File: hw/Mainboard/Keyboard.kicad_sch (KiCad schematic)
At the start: 8 parts, among them J18 KEYBOARD, J19 KEYBOARD_EX, U19 74LS145

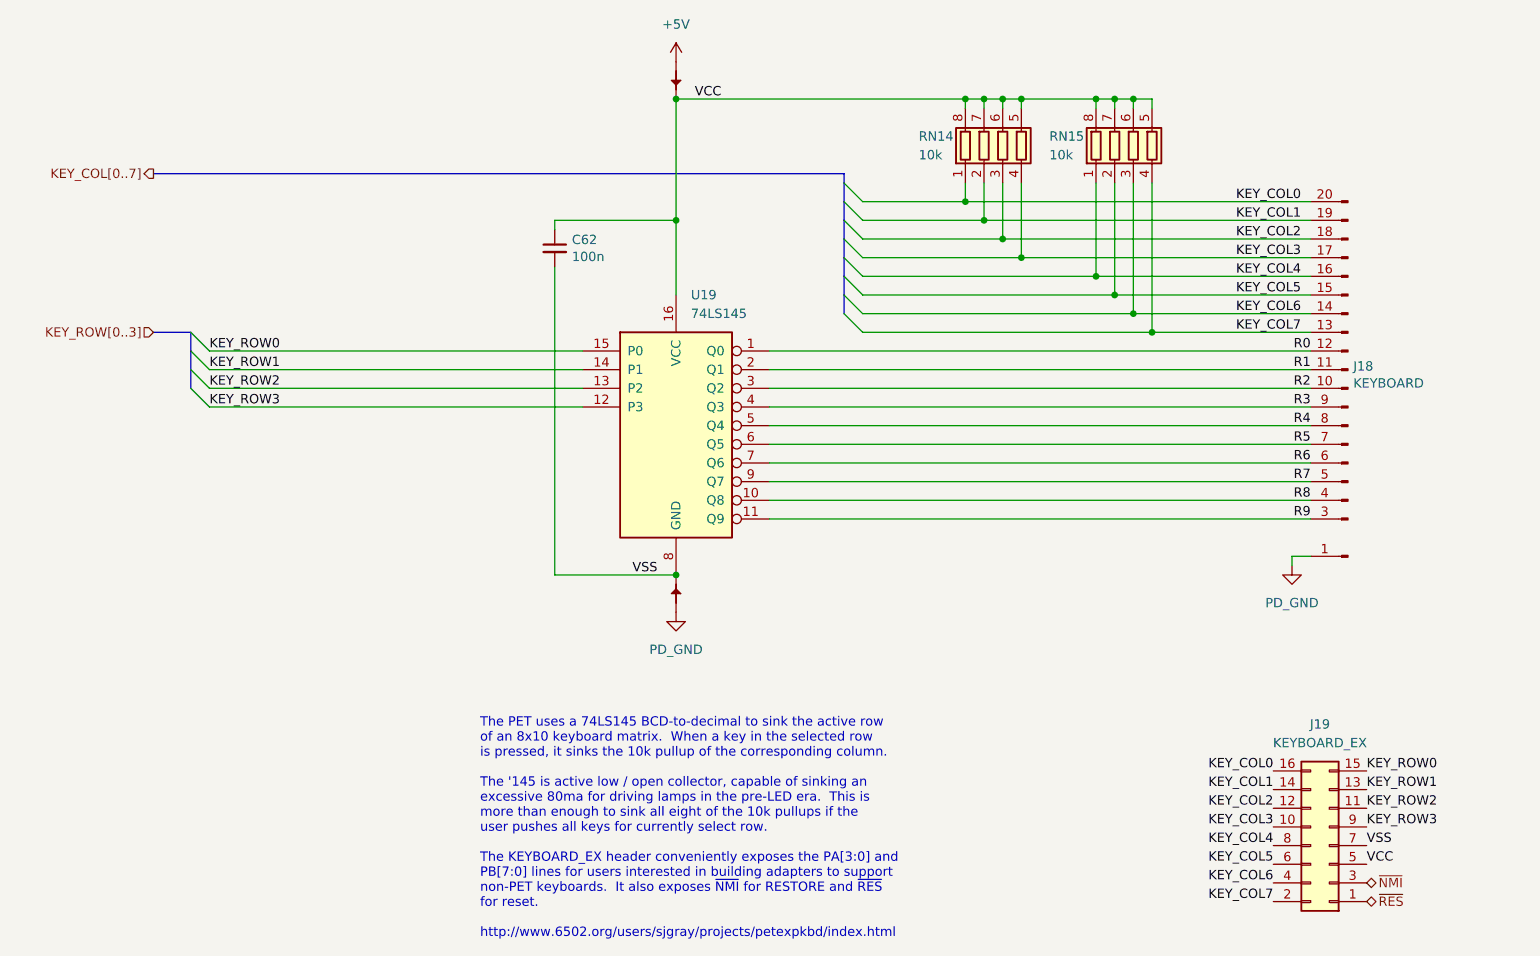
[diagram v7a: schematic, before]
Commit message: hw: 5V decoupling caps, routing touch ups (wip)
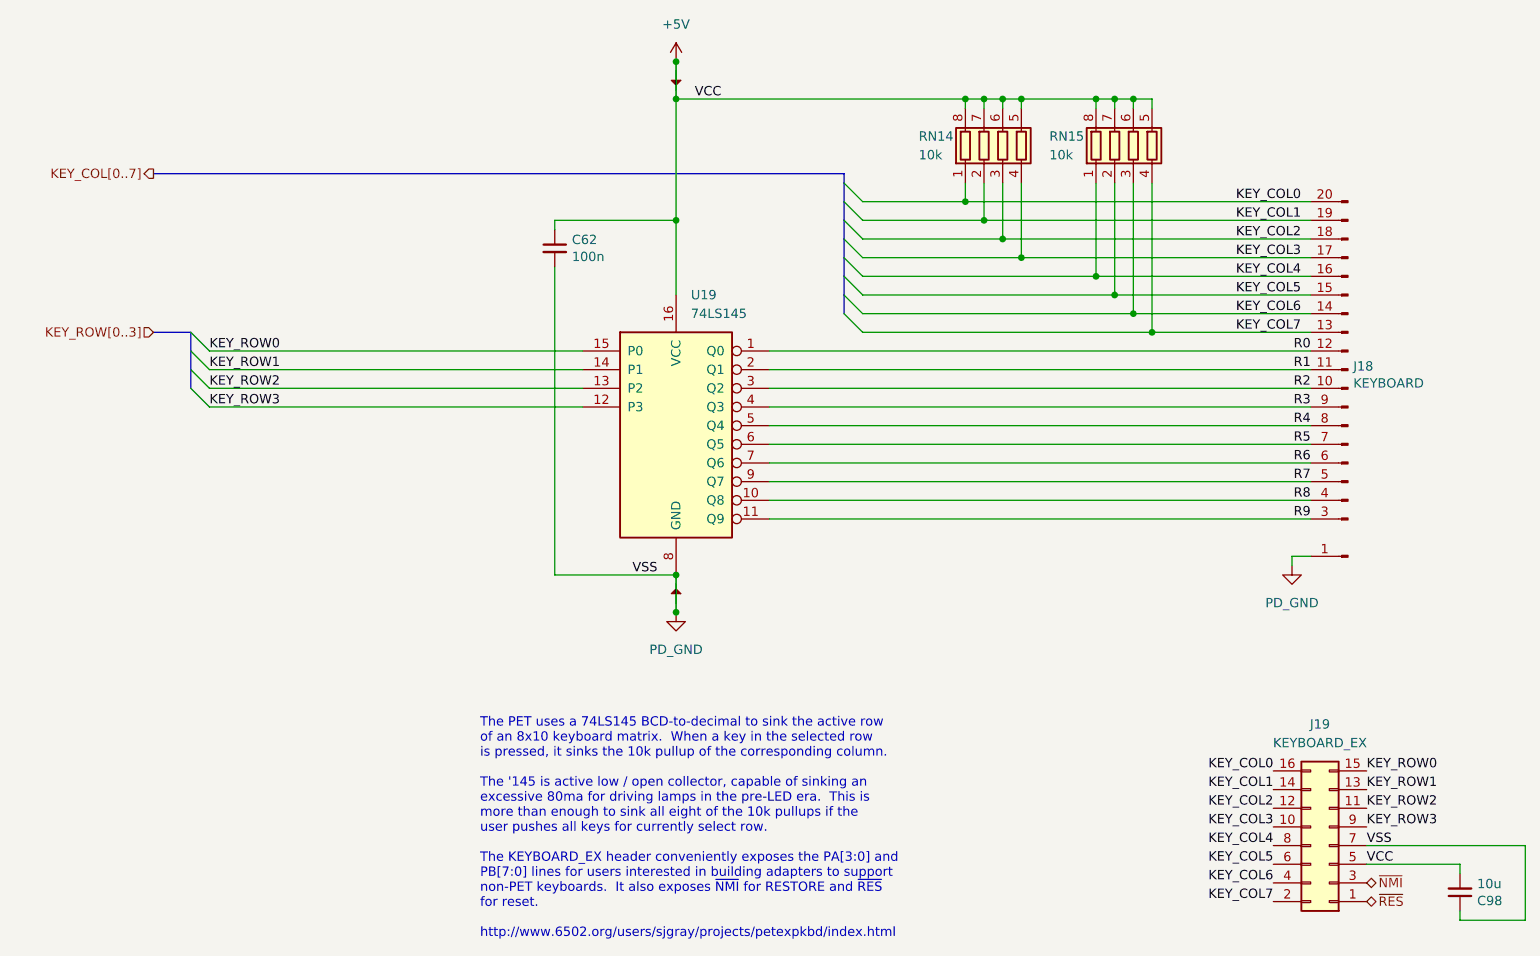
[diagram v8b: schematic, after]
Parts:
- added C98: 10u, Capacitor_SMD:C_0603_1608Metric, symbol Device:C_Small
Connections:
- net VCC is gone; now on net +5V: C62.1, J19.5 (Pin_5), PT42.2, RN14.5 (R4.2), RN14.6 (R3.2), RN14.7 (R2.2), RN14.8 (R1.2), RN15.5 (R4.2), RN15.6 (R3.2), RN15.7 (R2.2), RN15.8 (R1.2), U19.16 (VCC)
- net VSS is gone; now on net PD_GND: C62.2, J19.7 (Pin_7), PT43.2, U19.8 (GND)
- net +5V: now also C98.2
- net PD_GND: now also C98.1
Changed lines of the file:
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@@
   (junction (at 110.49 50.8) (diameter 0) (color 0 0 0 0)
   )
+  (junction (at 110.49 29.21) (diameter 0) (color 0 0 0 0)
+  )
   (junction (at 167.64 34.29) (diameter 0) (color 0 0 0 0)
   )
@@
   (junction (at 154.94 34.29) (diameter 0) (color 0 0 0 0)
   )
+  (junction (at 110.49 104.14) (diameter 0) (color 0 0 0 0)
+  )
   (junction (at 175.26 66.04) (diameter 0) (color 0 0 0 0)
   )
@@
     (stroke (width 0) (type default) (color 0 0 0 0))
   )
+  (wire (pts (xy 226.06 146.05) (xy 217.17 146.05))
+    (stroke (width 0) (type default) (color 0 0 0 0))
+  )
+  (wire (pts (xy 204.47 138.43) (xy 217.17 138.43))
+    (stroke (width 0) (type default) (color 0 0 0 0))
+  )
   (wire (pts (xy 152.4 34.29) (xy 154.94 34.29))
     (stroke (width 0) (type default) (color 0 0 0 0))
@@
     (stroke (width 0) (type default) (color 0 0 0 0))
   )
+  (wire (pts (xy 110.49 29.21) (xy 110.49 34.29))
+    (stroke (width 0) (type default) (color 0 0 0 0))
+  )
   (wire (pts (xy 110.49 34.29) (xy 149.86 34.29))
     (stroke (width 0) (type default) (color 0 0 0 0))
   )
+  (wire (pts (xy 204.47 135.89) (xy 226.06 135.89))
+    (stroke (width 0) (type default) (color 0 0 0 0))
+  )
   (wire (pts (xy 123.19 68.58) (xy 196.85 68.58))
     (stroke (width 0) (type default) (color 0 0 0 0))
@@
     (stroke (width 0) (type default) (color 0 0 0 0))
   )
+  (wire (pts (xy 226.06 135.89) (xy 226.06 146.05))
+    (stroke (width 0) (type default) (color 0 0 0 0))
+  )
   (wire (pts (xy 135.89 53.34) (xy 154.94 53.34))
     (stroke (width 0) (type default) (color 0 0 0 0))
@@
     (stroke (width 0) (type default) (color 0 0 0 0))
   )
+  (wire (pts (xy 217.17 138.43) (xy 217.17 139.7))
+    (stroke (width 0) (type default) (color 0 0 0 0))
+  )
   (wire (pts (xy 46.99 68.58) (xy 97.79 68.58))
     (stroke (width 0) (type default) (color 0 0 0 0))
@@
     (stroke (width 0) (type default) (color 0 0 0 0))
   )
+  (wire (pts (xy 110.49 99.06) (xy 110.49 104.14))
+    (stroke (width 0) (type default) (color 0 0 0 0))
+  )
   (wire (pts (xy 123.19 71.12) (xy 196.85 71.12))
     (stroke (width 0) (type default) (color 0 0 0 0))
@@
   )
   (wire (pts (xy 93.98 57.15) (xy 93.98 99.06))
+    (stroke (width 0) (type default) (color 0 0 0 0))
+  )
+  (wire (pts (xy 217.17 146.05) (xy 217.17 144.78))
     (stroke (width 0) (type default) (color 0 0 0 0))
   )
@@
     (pin "1")
   )
+  (symbol (lib_id "Device:C_Small") (at 217.17 142.24 0) (mirror x) (unit 1)
+    (in_bom yes) (on_board yes)
+    (property "Reference" "C98" (id 0) (at 219.5068 143.4084 0)
+      (effects (font (size 1.27 1.27)) (justify left))
+    )
+    (property "Value" "10u" (id 1) (at 219.5068 141.097 0)
+      (effects (font (size 1.27 1.27)) (justify left))
+    )
+    (property "Footprint" "Capacitor_SMD:C_0603_1608Metric" (id 2) (at 217.17 142.24 0)
+      (effects (font (size 1.27 1.27)) hide)
+    )
+    (property "Datasheet" "https://datasheet.lcsc.com/lcsc/2304140030_Samsung-Electro-Mechanics-CL10A106MA8NRNC_C96446.pdf" (id 3) (at 217.17 142.24 0)
+      (effects (font (size 1.27 1.27)) hide)
+    )
+    (property "LCSC" "C96446" (id 4) (at 217.17 142.24 0)
+      (effects (font (size 1.27 1.27)) hide)
+    )
+    (pin "1")
+    (pin "2")
+  )
   (symbol (lib_id "power:+5V") (at 110.49 29.21 0) (unit 1)
